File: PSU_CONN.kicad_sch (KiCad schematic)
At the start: 1 part, among them J5 Conn_02x12_Counter_Clockwise

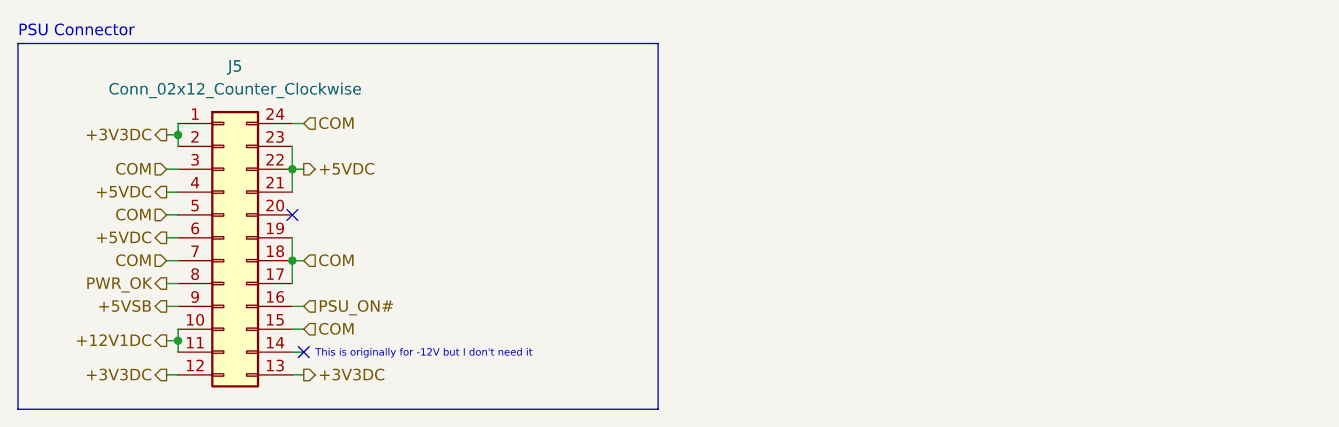
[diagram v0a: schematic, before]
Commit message: Transferred everything to hierarchical schematic and wired PSU power on circuit AND created duplicate schematics for all relevant subsystems
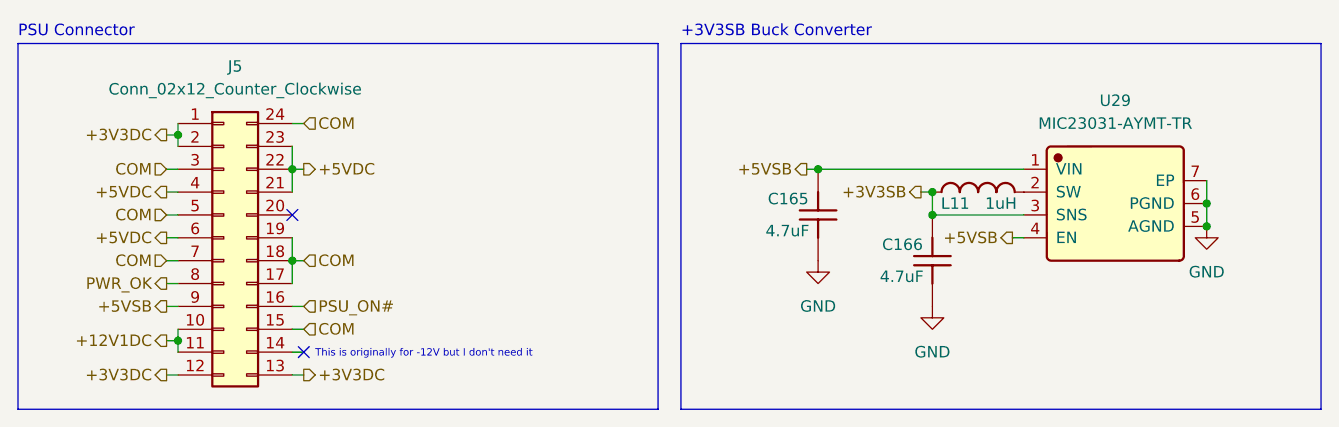
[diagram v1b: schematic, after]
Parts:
- added C165, C166: 4.7uF, Capacitor_SMD:C_0402_1005Metric, symbol JLCImport:CL05A475MP5NRNC
- added L11: 1uH, JLCImport:PIM201608S1R0MBCA, symbol JLCImport:PIM201608S1R0MBCA
- added U29: MIC23031-AYMT-TR, JLCImport:MIC23031-AYMT-TR, symbol JLCImport:MIC23031-AYMT-TR
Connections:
- net +5VSB: now also C165.2, U29.1 (VIN), U29.4 (EN)
- new net: L11.2, U29.2 (SW)
- new net +3V3SB: C166.2, L11.1, U29.3 (SNS)
- new net GND: C165.1, C166.1, U29.5 (AGND), U29.6 (PGND), U29.7 (EP)
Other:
- note added: "+3V3SB Buck Converter"

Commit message: Cleaned up schematic and replaced TC358743XBG with reverse-engineered LT6911C
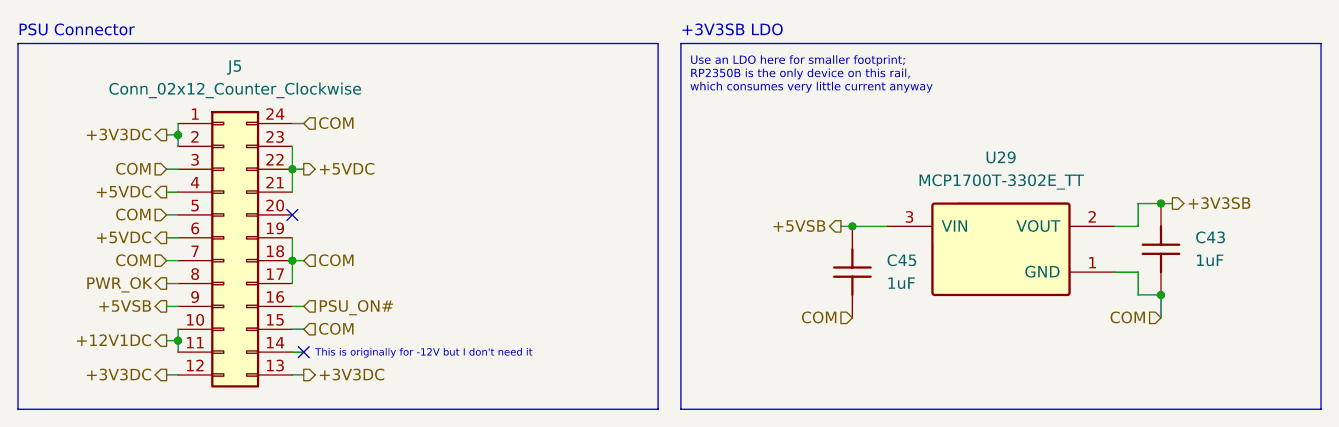
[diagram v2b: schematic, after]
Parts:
- removed C165, C166: 4.7uF, Capacitor_SMD:C_0402_1005Metric, symbol JLCImport:CL05A475MP5NRNC
- removed L11: 1uH, JLCImport:PIM201608S1R0MBCA, symbol JLCImport:PIM201608S1R0MBCA
- removed U29: MIC23031-AYMT-TR, JLCImport:MIC23031-AYMT-TR, symbol JLCImport:MIC23031-AYMT-TR
- added C43, C45: 1uF, Capacitor_SMD:C_0402_1005Metric, symbol JLCImport:CL05A105KA5NQNC
- added U29: MCP1700T-3302E_TT, JLCImport:MCP1700T-3302E_TT, symbol JLCImport:MCP1700T-3302E_TT
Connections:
- net +3V3SB: now also C43.2, U29.2 (VOUT)
- net +5VSB: now also C45.2, U29.3 (VIN)
- net COM: now also C43.1, C45.1, U29.1 (GND)
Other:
- note added: "+3V3SB LDO"
- note added: "Use an LDO here for smaller footprint; RP2350B is the only device on this rail, which consumes very little current anyway"
- note removed: "+3V3SB Buck Converter"
